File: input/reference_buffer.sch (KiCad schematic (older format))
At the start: 24 parts, among them Q1 NSS1C300ET4G, U3 OPA2210

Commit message: Mainly BOM changes to input board.
input:
Changed "DK line" attribute from plain "3" ti "I.3", reflecting the evolving interpretation of this as a part code.  This
causes all the input schematics to be modified.  Filled out some attributes

sma_breakout.sch: updated notes
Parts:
- C1, C2, C41: DK line 14 -> I.14; Manufacturer Murata Electronics -> GRM2195C1H103GA01D
- C3, C4: DK line 27 -> I.27
- C42: DK line (none) -> M.6; Description (none) -> CAP FILM 3.3UF 5% 63VDC RADIAL
- C5: DK line 19 -> I.19
- D1, D2: DK line 43 -> I.43
- Q1: DK line 23 -> I.23
- R1, R2, R3, R36, R4: DK line 17 -> I.17
- R14, R5: DK line 50 -> I.50
- R37: DK line (none) -> I.53; Description (none) -> 3.3 kOhms ±1% 0.1W, 1/10W Chip Resistor 0603 (1608 Metric) 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; Digikey (none) -> YAG3354CT-ND; MPN (none) -> RT0603FRE073K3L; Manufacturer (none) -> Yageo
- R38: DK line (none) -> M.12; Description ? -> RES 0 OHM JUMPER 1/10W 0603; Digikey (none) -> RMCF0603ZT0R00CT-ND; MPN (none) -> RMCF0603ZT0R00; Manufacturer (none) -> Stackpole Electronics Inc
- R5: DK line 10 -> I.10
- R6: DK line 16 -> I.16
- U3: DK line (none) -> D.1; Digikey (none) -> 296-OPA2210IDRCT-ND; MPN (none) -> OPA2210IDR; Manufacturer (none) -> Texas Instruments
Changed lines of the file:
@@
 F 5 "1276-6471-1-ND" H 4950 4400 50  0001 C CNN "Digikey"
 F 6 "CL21B105KOFNNNG" H 4950 4400 50  0001 C CNN "MPN"
-F 7 "27" H 4950 4400 50  0001 C CNN "DK line"
+F 7 "I.27" H 4950 4400 50  0001 C CNN "DK line"
 F 8 "Samsung Electro-Mechanics" H 4950 4400 50  0001 C CNN "Manufacturer"
 	1    4950 4400
@@
 F 5 "1276-6471-1-ND" H 4950 5250 50  0001 C CNN "Digikey"
 F 6 "CL21B105KOFNNNG" H 4950 5250 50  0001 C CNN "MPN"
-F 7 "27" H 4950 5250 50  0001 C CNN "DK line"
+F 7 "I.27" H 4950 5250 50  0001 C CNN "DK line"
 F 8 "Samsung Electro-Mechanics" H 4950 5250 50  0001 C CNN "Manufacturer"
 	1    4950 5250
@@
 F 3 "https://industrial.panasonic.com/cdbs/www-data/pdf/RDM0000/AOA0000C307.pdf" H 7800 2500 50  0001 C CNN
 F 4 "0.1%" V 7800 2500 50  0001 C CNN "Notes"
-F 5 "17" H 7800 2500 50  0001 C CNN "DK line"
+F 5 "I.17" H 7800 2500 50  0001 C CNN "DK line"
 F 6 "RES 2K OHM 0.1% 1/8W 0805" H 7800 2500 50  0001 C CNN "Description"
 F 7 "P2.0KDACT-ND" H 7800 2500 50  0001 C CNN "Digikey"
@@
 F 6 "490-8296-1-ND" H 7550 2900 50  0001 C CNN "Digikey"
 F 7 "GRM2195C1H103GA01D" H 7550 2900 50  0001 C CNN "MPN"
-F 8 "14" H 7550 2900 50  0001 C CNN "DK line"
-F 9 "Murata Electronics" H 7550 2900 50  0001 C CNN "Manufacturer"
+F 8 "I.14" H 7550 2900 50  0001 C CNN "DK line"
+F 9 "GRM2195C1H103GA01D" H 7550 2900 50  0001 C CNN "Manufacturer"
 	1    7550 2900
 	0    1    -1   0
@@
 F 2 "Resistor_SMD:R_1206_3216Metric" V 10740 3840 50  0001 C CNN
 F 3 "https://www.yageo.com/upload/media/product/productsearch/datasheet/rchip/PYu-RL_Group_521_RoHS_L_2.pdf" H 10700 3850 50  0001 C CNN
-F 4 "10" H 10700 3850 50  0001 C CNN "DK line"
+F 4 "I.10" H 10700 3850 50  0001 C CNN "DK line"
 F 5 "RES 0.068 OHM 1% 1/4W 1206" H 10700 3850 50  0001 C CNN "Description"
 F 6 "311-.068LWCT-ND" H 10700 3850 50  0001 C CNN "Digikey"
@@
 F 3 "https://industrial.panasonic.com/cdbs/www-data/pdf/RDM0000/AOA0000C307.pdf" H 2850 5400 50  0001 C CNN
 F 4 "0.1%" V 2850 5400 50  0001 C CNN "Notes"
-F 5 "17" H 2850 5400 50  0001 C CNN "DK line"
+F 5 "I.17" H 2850 5400 50  0001 C CNN "DK line"
 F 6 "RES 2K OHM 0.1% 1/8W 0805" H 2850 5400 50  0001 C CNN "Description"
 F 7 "P2.0KDACT-ND" H 2850 5400 50  0001 C CNN "Digikey"
@@
 F 3 "https://industrial.panasonic.com/cdbs/www-data/pdf/RDM0000/AOA0000C307.pdf" H 2300 3400 50  0001 C CNN
 F 4 "0.1%" V 2300 3400 50  0001 C CNN "Notes"
-F 5 "17" H 2300 3400 50  0001 C CNN "DK line"
+F 5 "I.17" H 2300 3400 50  0001 C CNN "DK line"
 F 6 "RES 2K OHM 0.1% 1/8W 0805" H 2300 3400 50  0001 C CNN "Description"
 F 7 "P2.0KDACT-ND" H 2300 3400 50  0001 C CNN "Digikey"
@@
 F 3 "https://industrial.panasonic.com/cdbs/www-data/pdf/RDM0000/AOA0000C307.pdf" H 2350 4900 50  0001 C CNN
 F 4 "0.1%" V 2350 4900 50  0001 C CNN "Notes"
-F 5 "17" H 2350 4900 50  0001 C CNN "DK line"
+F 5 "I.17" H 2350 4900 50  0001 C CNN "DK line"
 F 6 "RES 2K OHM 0.1% 1/8W 0805" H 2350 4900 50  0001 C CNN "Description"
 F 7 "P2.0KDACT-ND" H 2350 4900 50  0001 C CNN "Digikey"
@@
 F 6 "490-8296-1-ND" H 3350 5400 50  0001 C CNN "Digikey"
 F 7 "GRM2195C1H103GA01D" H 3350 5400 50  0001 C CNN "MPN"
-F 8 "14" H 3350 5400 50  0001 C CNN "DK line"
-F 9 "Murata Electronics" H 3350 5400 50  0001 C CNN "Manufacturer"
+F 8 "I.14" H 3350 5400 50  0001 C CNN "DK line"
+F 9 "GRM2195C1H103GA01D" H 3350 5400 50  0001 C CNN "Manufacturer"
 	1    3350 5400
 	-1   0    0    1
@@
 F 2 "Resistor_SMD:R_1206_3216Metric" V 9690 4240 50  0001 C CNN
 F 3 "http://www.koaspeer.com/catimages/Products/RK73H/RK73H.pdf" H 9650 4250 50  0001 C CNN
-F 4 "16" H 9650 4250 50  0001 C CNN "DK line"
+F 4 "I.16" H 9650 4250 50  0001 C CNN "DK line"
 F 5 "2.74 Ohms ±1% 0.25W, 1/4W Chip Resistor 1206 (3216 Metric) Automotive AEC-Q200, Moisture Resistant Thick Film" H 9650 4250 50  0001 C CNN "Description"
 F 6 "2019-RK73H2BTTD2R74FCT-ND" H 9650 4250 50  0001 C CNN "Digikey"
@@
 F 2 "Package_TO_SOT_SMD:SOT-23" H 8850 4350 50  0001 C CNN
 F 3 "http://www.onsemi.com/pub/Collateral/BAS21SLT1-D.PDF" H 8850 4600 50  0001 C CNN
-F 4 "43" H 8850 4500 50  0001 C CNN "DK line"
+F 4 "I.43" H 8850 4500 50  0001 C CNN "DK line"
 F 5 "DIODE ARRAY GP 250V 225MA SOT23" H 8850 4500 50  0001 C CNN "Description"
 F 6 "BAS21SLT1GOSCT-ND" H 8850 4500 50  0001 C CNN "Digikey"
@@
 F 2 "Package_TO_SOT_SMD:SOT-23" H 9300 4000 50  0001 C CNN
 F 3 "http://www.onsemi.com/pub/Collateral/BAS21SLT1-D.PDF" H 9300 4250 50  0001 C CNN
-F 4 "43" H 9300 4150 50  0001 C CNN "DK line"
+F 4 "I.43" H 9300 4150 50  0001 C CNN "DK line"
 F 5 "DIODE ARRAY GP 250V 225MA SOT23" H 9300 4150 50  0001 C CNN "Description"
 F 6 "BAS21SLT1GOSCT-ND" H 9300 4150 50  0001 C CNN "Digikey"
@@
 F 2 "Package_TO_SOT_SMD:SOT-23" H 9300 4350 50  0001 C CNN
 F 3 "http://www.onsemi.com/pub/Collateral/BAS21SLT1-D.PDF" H 9300 4600 50  0001 C CNN
-F 4 "43" H 9300 4500 50  0001 C CNN "DK line"
+F 4 "I.43" H 9300 4500 50  0001 C CNN "DK line"
 F 5 "DIODE ARRAY GP 250V 225MA SOT23" H 9300 4500 50  0001 C CNN "Description"
 F 6 "BAS21SLT1GOSCT-ND" H 9300 4500 50  0001 C CNN "Digikey"
@@
 F 4 "TRANS PNP 100V 3A 3DPAK" H 9550 4700 50  0001 C CNN "Description"
 F 5 "NSS1C300ET4GOSCT-ND" H 9550 4700 50  0001 C CNN "Digikey"
-F 6 "23" H 9550 4700 50  0001 C CNN "DK line"
+F 6 "I.23" H 9550 4700 50  0001 C CNN "DK line"
 F 7 "NSS1C300ET4G" H 9550 4700 50  0001 C CNN "MPN"
 F 8 "ON Semiconductor" H 9550 4700 50  0001 C CNN "Manufacturer"
@@
 F 3 "https://industrial.panasonic.com/cdbs/www-data/pdf/RDM0000/AOA0000C307.pdf" H 5300 3400 50  0001 C CNN
 F 4 "0.1%" V 5300 3400 50  0001 C CNN "Notes"
-F 5 "17" H 5300 3400 50  0001 C CNN "DK line"
+F 5 "I.17" H 5300 3400 50  0001 C CNN "DK line"
 F 6 "RES 2K OHM 0.1% 1/8W 0805" H 5300 3400 50  0001 C CNN "Description"
 F 7 "P2.0KDACT-ND" H 5300 3400 50  0001 C CNN "Digikey"
@@
 F 6 "490-8296-1-ND" H 5300 3750 50  0001 C CNN "Digikey"
 F 7 "GRM2195C1H103GA01D" H 5300 3750 50  0001 C CNN "MPN"
-F 8 "14" H 5300 3750 50  0001 C CNN "DK line"
-F 9 "Murata Electronics" H 5300 3750 50  0001 C CNN "Manufacturer"
+F 8 "I.14" H 5300 3750 50  0001 C CNN "DK line"
+F 9 "GRM2195C1H103GA01D" H 5300 3750 50  0001 C CNN "Manufacturer"
 	1    5300 3750
 	0    -1   -1   0
@@
 F 2 "Resistor_SMD:R_0603_1608Metric" V 6140 4790 50  0001 C CNN
 F 3 "~" H 6100 4800 50  0001 C CNN
+F 4 "I.53" H 6100 4800 50  0001 C CNN "DK line"
+F 5 "3.3 kOhms ±1% 0.1W, 1/10W Chip Resistor 0603 (1608 Metric)  Thin Film" H 6100 4800 50  0001 C CNN "Description"
+F 6 "YAG3354CT-ND" H 6100 4800 50  0001 C CNN "Digikey"
+F 7 "RT0603FRE073K3L" H 6100 4800 50  0001 C CNN "MPN"
+F 8 "Yageo" H 6100 4800 50  0001 C CNN "Manufacturer"
 	1    6100 4800
 	0    1    1    0
@@
 F 5 "R60DF4330506AJ" V 6450 5200 50  0001 C CNN "MPN"
 F 6 "KEMET" V 6450 5200 50  0001 C CNN "Manufacturer"
+F 7 "M.6" H 6450 5200 50  0001 C CNN "DK line"
+F 8 "CAP FILM 3.3UF 5% 63VDC RADIAL" H 6450 5200 50  0001 C CNN "Description"
 	1    6450 5200
 	1    0    0    -1
@@
 F 3 "?" H 4800 5100 60  0001 L CNN
 F 4 "IC OPAMP 2 CIRCUIT" H 4800 5800 60  0001 L CNN "Description"
+F 5 "D.1" H 4600 4800 50  0001 C CNN "DK line"
+F 6 "296-OPA2210IDRCT-ND" H 4600 4800 50  0001 C CNN "Digikey"
+F 7 "OPA2210IDR" H 4600 4800 50  0001 C CNN "MPN"
+F 8 "Texas Instruments" H 4600 4800 50  0001 C CNN "Manufacturer"
 	1    4600 4800
 	1    0    0    -1
@@
 F 3 "?" H 7700 5000 60  0001 L CNN
 F 4 "IC OPAMP 2 CIRCUIT" H 7700 5700 60  0001 L CNN "Description"
+F 5 "D.1" H 7500 4700 50  0001 C CNN "DK line"
+F 6 "296-OPA2210IDRCT-ND" H 7500 4700 50  0001 C CNN "Digikey"
+F 7 "OPA2210IDR" H 7500 4700 50  0001 C CNN "MPN"
+F 8 "Texas Instruments" H 7500 4700 50  0001 C CNN "Manufacturer"
 	2    7500 4700
 	1    0    0    -1
@@
 F 3 "?" H 11000 6000 50  0001 C CNN
 F 4 "" V 11000 6000 50  0001 C CNN "Notes"
-F 5 "" H 11000 6000 50  0001 C CNN "DK line"
-F 6 "?" H 11000 6000 50  0001 C CNN "Description"
-F 7 "" H 11000 6000 50  0001 C CNN "Digikey"
-F 8 "" H 11000 6000 50  0001 C CNN "MPN"
-F 9 "" H 11000 6000 50  0001 C CNN "Manufacturer"
+F 5 "M.12" H 11000 6000 50  0001 C CNN "DK line"
+F 6 "RES 0 OHM JUMPER 1/10W 0603" H 11000 6000 50  0001 C CNN "Description"
+F 7 "RMCF0603ZT0R00CT-ND" H 11000 6000 50  0001 C CNN "Digikey"
+F 8 "RMCF0603ZT0R00" H 11000 6000 50  0001 C CNN "MPN"
+F 9 "Stackpole Electronics Inc" H 11000 6000 50  0001 C CNN "Manufacturer"
 	1    11000 6000
 	0    1    -1   0
@@
 F 5 "APXG160ARA331MH70G" V 11650 4750 50  0001 C CNN "MPN"
 F 6 "16V aluminum solid polymer, ESR 22 mOhm" V 11650 4750 50  0001 C CNN "Description"
-F 7 "19" H 11650 4750 50  0001 C CNN "DK line"
+F 7 "I.19" H 11650 4750 50  0001 C CNN "DK line"
 F 8 "United Chemi-Con" H 11650 4750 50  0001 C CNN "Manufacturer"
 	1    11650 4750
@@
 F 3 "~" H 9650 3550 50  0001 C CNN
 F 4 "0.1%" V 9650 3550 50  0001 C CNN "Notes"
-F 5 "50" H 9650 3550 50  0001 C CNN "DK line"
+F 5 "I.50" H 9650 3550 50  0001 C CNN "DK line"
 F 6 "301 Ohms ±1% 0.125W, 1/8W Chip Resistor 0603 (1608 Metric) Anti-Sulfur, Moisture Resistant Thin Film" H 9650 3550 50  0001 C CNN "Description"
 F 7 "RNCP0603FTD301RCT-ND" H 9650 3550 50  0001 C CNN "Digikey"
@@
 F 3 "~" H 9250 3550 50  0001 C CNN
 F 4 "0.1%" V 9250 3550 50  0001 C CNN "Notes"
-F 5 "50" H 9250 3550 50  0001 C CNN "DK line"
+F 5 "I.50" H 9250 3550 50  0001 C CNN "DK line"
 F 6 "301 Ohms ±1% 0.125W, 1/8W Chip Resistor 0603 (1608 Metric) Anti-Sulfur, Moisture Resistant Thin Film" H 9250 3550 50  0001 C CNN "Description"
 F 7 "RNCP0603FTD301RCT-ND" H 9250 3550 50  0001 C CNN "Digikey"

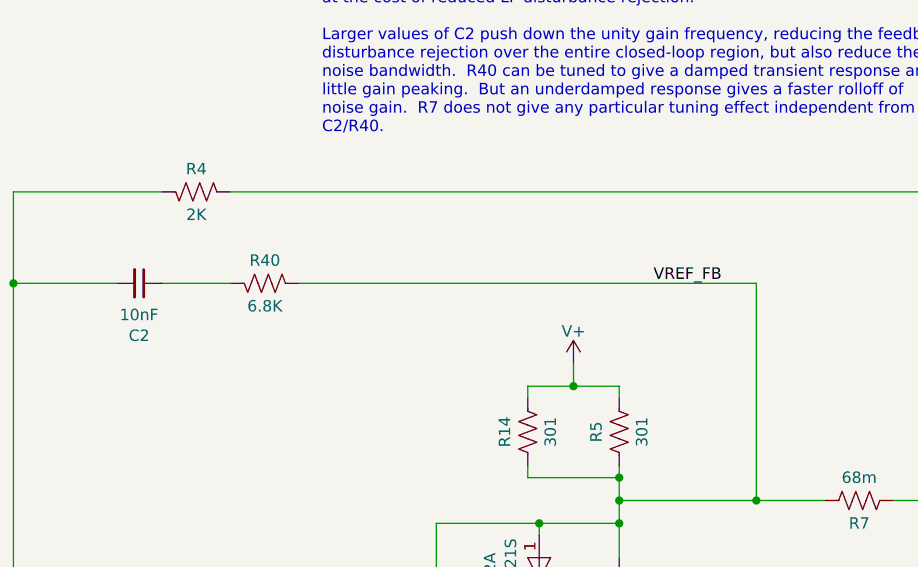
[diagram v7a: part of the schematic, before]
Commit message: Input board R1 being sent to fab.  Changes related to BOM reconciliation with the Digikey BOM.  This includes a couple of fixes to the footprint which affected the layout, as well as a couple changes to series connect resistors to avoid a new unique part.
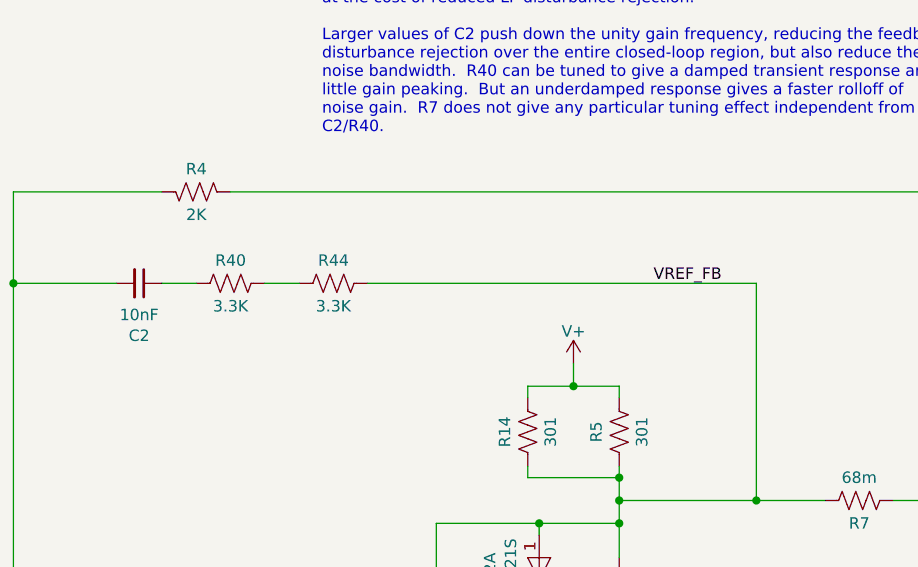
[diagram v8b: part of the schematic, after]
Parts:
- added R44: 3.3K, Resistor_SMD:R_0603_1608Metric, symbol Device:R_US
- C1, C2, C41: Manufacturer GRM2195C1H103GA01D -> Murata Electronics
- R1, R2, R3, R36, R4: footprint Resistor_SMD:R_0603_1608Metric -> Resistor_SMD:R_0805_2012Metric
- R14, R5: footprint Resistor_SMD:R_0805_2012Metric -> Resistor_SMD:R_0603_1608Metric; Notes 0.1% -> (none)
- R40: value 6.8K -> 3.3K; DK line (none) -> I.53; Description (none) -> 3.3 kOhms ±1% 0.1W, 1/10W Chip Resistor 0603 (1608 Metric) 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; Digikey (none) -> YAG3354CT-ND; MPN (none) -> RT0603FRE073K3L; Manufacturer (none) -> Yageo
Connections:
- net VREF_FB: now also R44.2; no longer R40.1
- net at C2.1: now also R40.1; no longer R40.2
- new net: R40.2, R44.1
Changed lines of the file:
@@
 F 0 "R4" V 7900 2500 50  0000 C CNN
 F 1 "2K" V 7700 2500 50  0000 C CNN
-F 2 "Resistor_SMD:R_0603_1608Metric" V 7840 2490 50  0001 C CNN
+F 2 "Resistor_SMD:R_0805_2012Metric" V 7840 2490 50  0001 C CNN
 F 3 "https://industrial.panasonic.com/cdbs/www-data/pdf/RDM0000/AOA0000C307.pdf" H 7800 2500 50  0001 C CNN
 F 4 "0.1%" V 7800 2500 50  0001 C CNN "Notes"
@@
 F 7 "GRM2195C1H103GA01D" H 7550 2900 50  0001 C CNN "MPN"
 F 8 "I.14" H 7550 2900 50  0001 C CNN "DK line"
-F 9 "GRM2195C1H103GA01D" H 7550 2900 50  0001 C CNN "Manufacturer"
+F 9 "Murata Electronics" H 7550 2900 50  0001 C CNN "Manufacturer"
 	1    7550 2900
 	0    1    -1   0
@@
 F 0 "R3" V 2950 5400 50  0000 C CNN
 F 1 "2K" V 2750 5400 50  0000 C CNN
-F 2 "Resistor_SMD:R_0603_1608Metric" V 2890 5390 50  0001 C CNN
+F 2 "Resistor_SMD:R_0805_2012Metric" V 2890 5390 50  0001 C CNN
 F 3 "https://industrial.panasonic.com/cdbs/www-data/pdf/RDM0000/AOA0000C307.pdf" H 2850 5400 50  0001 C CNN
 F 4 "0.1%" V 2850 5400 50  0001 C CNN "Notes"
@@
 F 0 "R2" V 2400 3400 50  0000 C CNN
 F 1 "2K" V 2200 3400 50  0000 C CNN
-F 2 "Resistor_SMD:R_0603_1608Metric" V 2340 3390 50  0001 C CNN
+F 2 "Resistor_SMD:R_0805_2012Metric" V 2340 3390 50  0001 C CNN
 F 3 "https://industrial.panasonic.com/cdbs/www-data/pdf/RDM0000/AOA0000C307.pdf" H 2300 3400 50  0001 C CNN
 F 4 "0.1%" V 2300 3400 50  0001 C CNN "Notes"
@@
 F 0 "R1" V 2450 4900 50  0000 C CNN
 F 1 "2K" V 2250 4900 50  0000 C CNN
-F 2 "Resistor_SMD:R_0603_1608Metric" V 2390 4890 50  0001 C CNN
+F 2 "Resistor_SMD:R_0805_2012Metric" V 2390 4890 50  0001 C CNN
 F 3 "https://industrial.panasonic.com/cdbs/www-data/pdf/RDM0000/AOA0000C307.pdf" H 2350 4900 50  0001 C CNN
 F 4 "0.1%" V 2350 4900 50  0001 C CNN "Notes"
@@
 F 7 "GRM2195C1H103GA01D" H 3350 5400 50  0001 C CNN "MPN"
 F 8 "I.14" H 3350 5400 50  0001 C CNN "DK line"
-F 9 "GRM2195C1H103GA01D" H 3350 5400 50  0001 C CNN "Manufacturer"
+F 9 "Murata Electronics" H 3350 5400 50  0001 C CNN "Manufacturer"
 	1    3350 5400
 	-1   0    0    1
@@
 F 0 "R36" V 5400 3400 50  0000 C CNN
 F 1 "2K" V 5200 3400 50  0000 C CNN
-F 2 "Resistor_SMD:R_0603_1608Metric" V 5340 3390 50  0001 C CNN
+F 2 "Resistor_SMD:R_0805_2012Metric" V 5340 3390 50  0001 C CNN
 F 3 "https://industrial.panasonic.com/cdbs/www-data/pdf/RDM0000/AOA0000C307.pdf" H 5300 3400 50  0001 C CNN
 F 4 "0.1%" V 5300 3400 50  0001 C CNN "Notes"
@@
 F 7 "GRM2195C1H103GA01D" H 5300 3750 50  0001 C CNN "MPN"
 F 8 "I.14" H 5300 3750 50  0001 C CNN "DK line"
-F 9 "GRM2195C1H103GA01D" H 5300 3750 50  0001 C CNN "Manufacturer"
+F 9 "Murata Electronics" H 5300 3750 50  0001 C CNN "Manufacturer"
 	1    5300 3750
 	0    -1   -1   0
@@
 Wire Wire Line
 	5750 3750 5750 4800
-$Comp
-L Device:R_US R?
-U 1 1 602064F3
-P 8100 2900
-AR Path="/5DFF6C0D/602064F3" Ref="R?"  Part="1"
-AR Path="/5E1D6729/5E1DA2AA/602064F3" Ref="R?"  Part="1"
-AR Path="/5E2EB92B/602064F3" Ref="R40"  Part="1"
-AR Path="/5E624B3C/5E2EB92B/602064F3" Ref="R?"  Part="1"
-AR Path="/5EBEDCCA/602064F3" Ref="R?"  Part="1"
-F 0 "R40" V 8200 2900 50  0000 C CNN
-F 1 "6.8K" V 8000 2900 50  0000 C CNN
-F 2 "Resistor_SMD:R_0603_1608Metric" V 8140 2890 50  0001 C CNN
-F 3 "~" H 8100 2900 50  0001 C CNN
-	1    8100 2900
-	0    1    -1   0
-$EndComp
-Wire Wire Line
-	10250 2900 8250 2900
-Wire Wire Line
-	7950 2900 7650 2900
+Wire Wire Line
+	10250 2900 8550 2900
 Wire Wire Line
 	7450 2900 7000 2900
@@
 F 0 "R5" V 9750 3550 50  0000 C CNN
 F 1 "301" V 9550 3550 50  0000 C CNN
-F 2 "Resistor_SMD:R_0805_2012Metric" V 9690 3540 50  0001 C CNN
-F 3 "~" H 9650 3550 50  0001 C CNN
-F 4 "0.1%" V 9650 3550 50  0001 C CNN "Notes"
+F 2 "Resistor_SMD:R_0603_1608Metric" V 9690 3540 50  0001 C CNN
+F 3 "https://www.seielect.com/catalog/sei-rncp.pdf" H 9650 3550 50  0001 C CNN
+F 4 "" V 9650 3550 50  0001 C CNN "Notes"
 F 5 "I.50" H 9650 3550 50  0001 C CNN "DK line"
 F 6 "301 Ohms ±1% 0.125W, 1/8W Chip Resistor 0603 (1608 Metric) Anti-Sulfur, Moisture Resistant Thin Film" H 9650 3550 50  0001 C CNN "Description"
@@
 F 0 "R14" V 9350 3550 50  0000 C CNN
 F 1 "301" V 9150 3550 50  0000 C CNN
-F 2 "Resistor_SMD:R_0805_2012Metric" V 9290 3540 50  0001 C CNN
-F 3 "~" H 9250 3550 50  0001 C CNN
-F 4 "0.1%" V 9250 3550 50  0001 C CNN "Notes"
+F 2 "Resistor_SMD:R_0603_1608Metric" V 9290 3540 50  0001 C CNN
+F 3 "https://www.seielect.com/catalog/sei-rncp.pdf" H 9250 3550 50  0001 C CNN
+F 4 "" V 9250 3550 50  0001 C CNN "Notes"
 F 5 "I.50" H 9250 3550 50  0001 C CNN "DK line"
 F 6 "301 Ohms ±1% 0.125W, 1/8W Chip Resistor 0603 (1608 Metric) Anti-Sulfur, Moisture Resistant Thin Film" H 9250 3550 50  0001 C CNN "Description"
@@
 	-1   0    0    1
 $EndComp
+$Comp
+L Device:R_US R?
+U 1 1 60371540
+P 8400 2900
+AR Path="/5DFCF14D/5DE6CDF8/60371540" Ref="R?"  Part="1"
+AR Path="/5E448095/5DE6CDF8/60371540" Ref="R?"  Part="1"
+AR Path="/5E45936E/5DE6CDF8/60371540" Ref="R?"  Part="1"
+AR Path="/5E525F2C/5E6427A0/5DE6CDF8/60371540" Ref="R?"  Part="1"
+AR Path="/5E624B3C/5DFCF14D/5DE6CDF8/60371540" Ref="R?"  Part="1"
+AR Path="/5E624B3C/5E448095/5DE6CDF8/60371540" Ref="R?"  Part="1"
+AR Path="/5E624B3C/5E45936E/5DE6CDF8/60371540" Ref="R?"  Part="1"
+AR Path="/5E62FD57/5DFCF14D/5DE6CDF8/60371540" Ref="R?"  Part="1"
+AR Path="/5E62FD57/5E448095/5DE6CDF8/60371540" Ref="R?"  Part="1"
+AR Path="/5E62FD57/5E45936E/5DE6CDF8/60371540" Ref="R?"  Part="1"
+AR Path="/5E2EB92B/60371540" Ref="R44"  Part="1"
+F 0 "R44" V 8500 2900 50  0000 C CNN
+F 1 "3.3K" V 8300 2900 50  0000 C CNN
+F 2 "Resistor_SMD:R_0603_1608Metric" V 8440 2890 50  0001 C CNN
+F 3 "~" H 8400 2900 50  0001 C CNN
+F 4 "" H 8400 2900 50  0001 C CNN "Notes"
+F 5 "I.53" H 8400 2900 50  0001 C CNN "DK line"
+F 6 "3.3 kOhms ±1% 0.1W, 1/10W Chip Resistor 0603 (1608 Metric)  Thin Film" H 8400 2900 50  0001 C CNN "Description"
+F 7 "YAG3354CT-ND" H 8400 2900 50  0001 C CNN "Digikey"
+F 8 "RT0603FRE073K3L" H 8400 2900 50  0001 C CNN "MPN"
+F 9 "Yageo" H 8400 2900 50  0001 C CNN "Manufacturer"
+	1    8400 2900
+	0    -1   -1   0
+$EndComp
+$Comp
+L Device:R_US R?
+U 1 1 60377492
+P 7950 2900
+AR Path="/5DFCF14D/5DE6CDF8/60377492" Ref="R?"  Part="1"
+AR Path="/5E448095/5DE6CDF8/60377492" Ref="R?"  Part="1"
+AR Path="/5E45936E/5DE6CDF8/60377492" Ref="R?"  Part="1"
+AR Path="/5E525F2C/5E6427A0/5DE6CDF8/60377492" Ref="R?"  Part="1"
+AR Path="/5E624B3C/5DFCF14D/5DE6CDF8/60377492" Ref="R?"  Part="1"
+AR Path="/5E624B3C/5E448095/5DE6CDF8/60377492" Ref="R?"  Part="1"
+AR Path="/5E624B3C/5E45936E/5DE6CDF8/60377492" Ref="R?"  Part="1"
+AR Path="/5E62FD57/5DFCF14D/5DE6CDF8/60377492" Ref="R?"  Part="1"
+AR Path="/5E62FD57/5E448095/5DE6CDF8/60377492" Ref="R?"  Part="1"
+AR Path="/5E62FD57/5E45936E/5DE6CDF8/60377492" Ref="R?"  Part="1"
+AR Path="/5E2EB92B/60377492" Ref="R40"  Part="1"
+F 0 "R40" V 8050 2900 50  0000 C CNN
+F 1 "3.3K" V 7850 2900 50  0000 C CNN
+F 2 "Resistor_SMD:R_0603_1608Metric" V 7990 2890 50  0001 C CNN
+F 3 "~" H 7950 2900 50  0001 C CNN
+F 4 "" H 7950 2900 50  0001 C CNN "Notes"
+F 5 "I.53" H 7950 2900 50  0001 C CNN "DK line"
+F 6 "3.3 kOhms ±1% 0.1W, 1/10W Chip Resistor 0603 (1608 Metric)  Thin Film" H 7950 2900 50  0001 C CNN "Description"
+F 7 "YAG3354CT-ND" H 7950 2900 50  0001 C CNN "Digikey"
+F 8 "RT0603FRE073K3L" H 7950 2900 50  0001 C CNN "MPN"
+F 9 "Yageo" H 7950 2900 50  0001 C CNN "Manufacturer"
+	1    7950 2900
+	0    -1   -1   0
+$EndComp
+Wire Wire Line
+	7650 2900 7800 2900
+Wire Wire Line
+	8100 2900 8250 2900
 $EndSCHEMATC
